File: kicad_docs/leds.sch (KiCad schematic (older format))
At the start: 13 parts, among them U12 74HC595

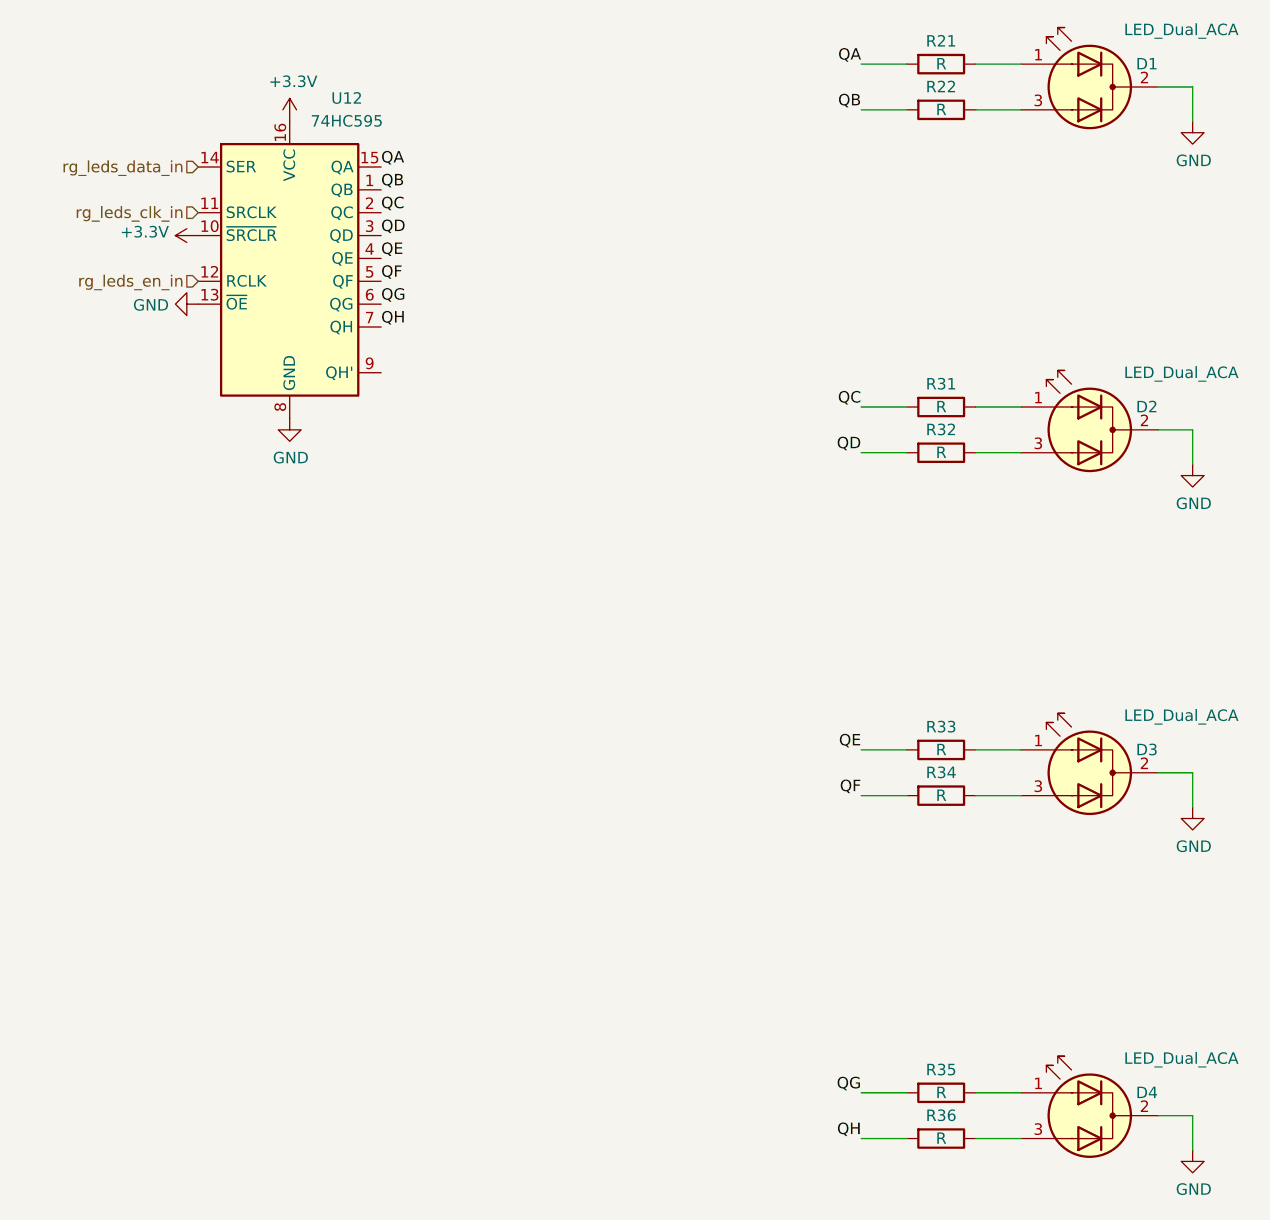
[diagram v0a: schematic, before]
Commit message: add EEPROM, big pcb re-design
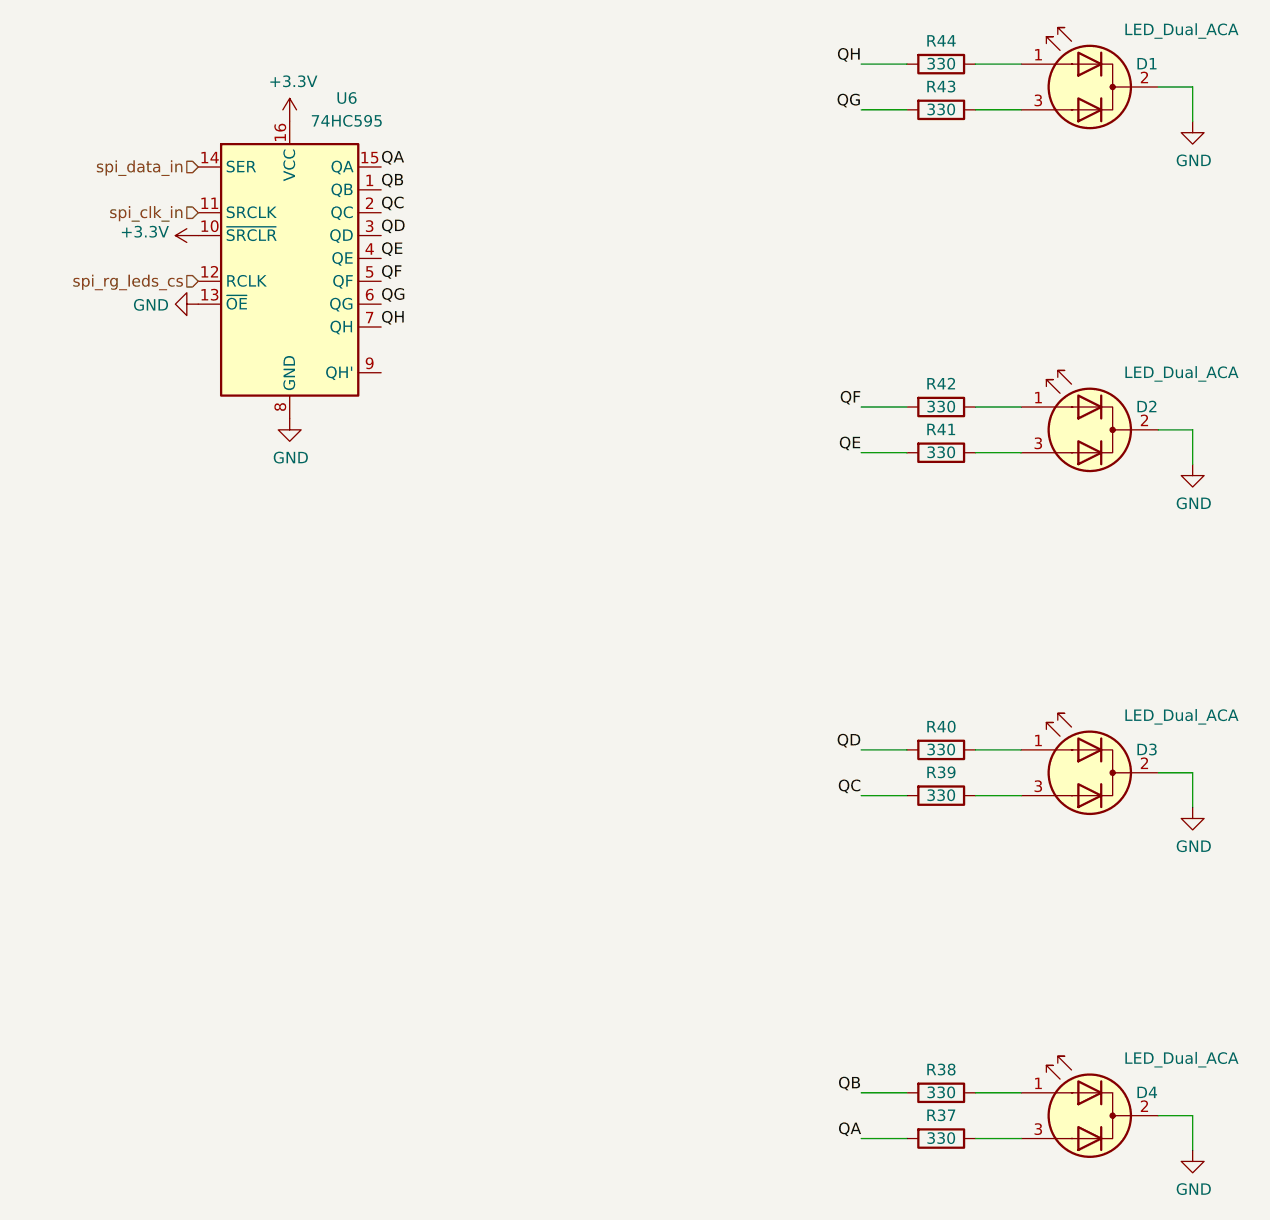
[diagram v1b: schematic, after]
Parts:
- R37: renamed from R21; value R -> 330; footprint Resistor_SMD:R_0805_2012Metric_Pad1.15x1.40mm_HandSolder -> Resistor_SMD:R_0603_1608Metric
- R38: renamed from R22; value R -> 330; footprint Resistor_SMD:R_0805_2012Metric_Pad1.15x1.40mm_HandSolder -> Resistor_SMD:R_0603_1608Metric
- R39: renamed from R31; value R -> 330; footprint Resistor_SMD:R_0805_2012Metric_Pad1.15x1.40mm_HandSolder -> Resistor_SMD:R_0603_1608Metric
- R40: renamed from R32; value R -> 330; footprint Resistor_SMD:R_0805_2012Metric_Pad1.15x1.40mm_HandSolder -> Resistor_SMD:R_0603_1608Metric
- R41: renamed from R33; value R -> 330; footprint Resistor_SMD:R_0805_2012Metric_Pad1.15x1.40mm_HandSolder -> Resistor_SMD:R_0603_1608Metric
- R42: renamed from R34; value R -> 330; footprint Resistor_SMD:R_0805_2012Metric_Pad1.15x1.40mm_HandSolder -> Resistor_SMD:R_0603_1608Metric
- R43: renamed from R35; value R -> 330; footprint Resistor_SMD:R_0805_2012Metric_Pad1.15x1.40mm_HandSolder -> Resistor_SMD:R_0603_1608Metric
- R44: renamed from R36; value R -> 330; footprint Resistor_SMD:R_0805_2012Metric_Pad1.15x1.40mm_HandSolder -> Resistor_SMD:R_0603_1608Metric
- renumbered U12 to U6
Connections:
- net at D1.1 (A1): now also R44.1; no longer R37.1
- net at D1.3 (A2): now also R43.1; no longer R38.1
- net at D2.1 (A1): now also R42.1; no longer R39.1
- net at D2.3 (A2): now also R41.1; no longer R40.1
- net at D3.1 (A1): now also R40.1; no longer R41.1
- net at D3.3 (A2): now also R39.1; no longer R42.1
- net at D4.1 (A1): now also R38.1; no longer R43.1
- net at D4.3 (A2): now also R37.1; no longer R44.1
- net rg_leds_clk_in renamed spi_clk_in
- net rg_leds_data_in renamed spi_data_in
- net rg_leds_en_in renamed spi_rg_leds_cs
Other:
- moved on the sheet: R37, R38, R39, R40, R41, R42, R43, R44
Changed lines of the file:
@@
 $Descr A4 11693 8268
 encoding utf-8
-Sheet 4 9
+Sheet 10 10
 Title ""
 Date ""
@@
 $EndComp
 $Comp
-L Device:R R21
+L Device:R R37
 U 1 1 5E6471EE
+P 6000 6150
+F 0 "R37" V 5900 6150 50  0000 C CNN
+F 1 "330" V 6000 6150 50  0000 C CNN
+F 2 "Resistor_SMD:R_0603_1608Metric" V 5930 6150 50  0001 C CNN
+F 3 "~" H 6000 6150 50  0001 C CNN
+	1    6000 6150
+	0    1    1    0
+$EndComp
+$Comp
+L Device:R R38
+U 1 1 5E6477D0
+P 6000 5950
+F 0 "R38" V 5900 5950 50  0000 C CNN
+F 1 "330" V 6000 5950 50  0000 C CNN
+F 2 "Resistor_SMD:R_0603_1608Metric" V 5930 5950 50  0001 C CNN
+F 3 "~" H 6000 5950 50  0001 C CNN
+	1    6000 5950
+	0    1    1    0
+$EndComp
+Wire Wire Line
+	6350 1450 6150 1450
+Wire Wire Line
+	5850 6150 5650 6150
+Wire Wire Line
+	5650 5950 5850 5950
+Wire Wire Line
+	6150 1650 6350 1650
+$Comp
+L Device:R R39
+U 1 1 5E7B2863
+P 6000 4650
+F 0 "R39" V 5900 4650 50  0000 C CNN
+F 1 "330" V 6000 4650 50  0000 C CNN
+F 2 "Resistor_SMD:R_0603_1608Metric" V 5930 4650 50  0001 C CNN
+F 3 "~" H 6000 4650 50  0001 C CNN
+	1    6000 4650
+	0    1    1    0
+$EndComp
+$Comp
+L Device:R R40
+U 1 1 5E7B2869
+P 6000 4450
+F 0 "R40" V 5900 4450 50  0000 C CNN
+F 1 "330" V 6000 4450 50  0000 C CNN
+F 2 "Resistor_SMD:R_0603_1608Metric" V 5930 4450 50  0001 C CNN
+F 3 "~" H 6000 4450 50  0001 C CNN
+	1    6000 4450
+	0    1    1    0
+$EndComp
+Wire Wire Line
+	6350 2950 6150 2950
+Wire Wire Line
+	5850 4650 5650 4650
+Wire Wire Line
+	5650 4450 5850 4450
+Wire Wire Line
+	6150 3150 6350 3150
+$Comp
+L Device:R R41
+U 1 1 5E7B36D9
+P 6000 3150
+F 0 "R41" V 5900 3150 50  0000 C CNN
+F 1 "330" V 6000 3150 50  0000 C CNN
+F 2 "Resistor_SMD:R_0603_1608Metric" V 5930 3150 50  0001 C CNN
+F 3 "~" H 6000 3150 50  0001 C CNN
+	1    6000 3150
+	0    1    1    0
+$EndComp
+$Comp
+L Device:R R42
+U 1 1 5E7B36DF
+P 6000 2950
+F 0 "R42" V 5900 2950 50  0000 C CNN
+F 1 "330" V 6000 2950 50  0000 C CNN
+F 2 "Resistor_SMD:R_0603_1608Metric" V 5930 2950 50  0001 C CNN
+F 3 "~" H 6000 2950 50  0001 C CNN
+	1    6000 2950
+	0    1    1    0
+$EndComp
+Wire Wire Line
+	6350 4450 6150 4450
+Wire Wire Line
+	5850 3150 5650 3150
+Wire Wire Line
+	5650 2950 5850 2950
+Wire Wire Line
+	6150 4650 6350 4650
+$Comp
+L Device:R R43
+U 1 1 5E7B44F9
+P 6000 1650
+F 0 "R43" V 5900 1650 50  0000 C CNN
+F 1 "330" V 6000 1650 50  0000 C CNN
+F 2 "Resistor_SMD:R_0603_1608Metric" V 5930 1650 50  0001 C CNN
+F 3 "~" H 6000 1650 50  0001 C CNN
+	1    6000 1650
+	0    1    1    0
+$EndComp
+$Comp
+L Device:R R44
+U 1 1 5E7B44FF
 P 6000 1450
-F 0 "R21" V 5900 1450 50  0000 C CNN
-F 1 "R" V 6000 1450 50  0000 C CNN
-F 2 "Resistor_SMD:R_0805_2012Metric_Pad1.15x1.40mm_HandSolder" V 5930 1450 50  0001 C CNN
+F 0 "R44" V 5900 1450 50  0000 C CNN
+F 1 "330" V 6000 1450 50  0000 C CNN
+F 2 "Resistor_SMD:R_0603_1608Metric" V 5930 1450 50  0001 C CNN
 F 3 "~" H 6000 1450 50  0001 C CNN
 	1    6000 1450
 	0    1    1    0
 $EndComp
-$Comp
-L Device:R R22
-U 1 1 5E6477D0
-P 6000 1650
-F 0 "R22" V 5900 1650 50  0000 C CNN
-F 1 "R" V 6000 1650 50  0000 C CNN
-F 2 "Resistor_SMD:R_0805_2012Metric_Pad1.15x1.40mm_HandSolder" V 5930 1650 50  0001 C CNN
-F 3 "~" H 6000 1650 50  0001 C CNN
-	1    6000 1650
-	0    1    1    0
-$EndComp
-Wire Wire Line
-	6350 1450 6150 1450
-Wire Wire Line
-	5850 1450 5650 1450
-Wire Wire Line
-	5650 1650 5850 1650
-Wire Wire Line
-	6150 1650 6350 1650
-$Comp
-L Device:R R31
-U 1 1 5E7B2863
-P 6000 2950
-F 0 "R31" V 5900 2950 50  0000 C CNN
-F 1 "R" V 6000 2950 50  0000 C CNN
-F 2 "Resistor_SMD:R_0805_2012Metric_Pad1.15x1.40mm_HandSolder" V 5930 2950 50  0001 C CNN
-F 3 "~" H 6000 2950 50  0001 C CNN
-	1    6000 2950
-	0    1    1    0
-$EndComp
-$Comp
-L Device:R R32
-U 1 1 5E7B2869
-P 6000 3150
-F 0 "R32" V 5900 3150 50  0000 C CNN
-F 1 "R" V 6000 3150 50  0000 C CNN
-F 2 "Resistor_SMD:R_0805_2012Metric_Pad1.15x1.40mm_HandSolder" V 5930 3150 50  0001 C CNN
-F 3 "~" H 6000 3150 50  0001 C CNN
-	1    6000 3150
-	0    1    1    0
-$EndComp
-Wire Wire Line
-	6350 2950 6150 2950
-Wire Wire Line
-	5850 2950 5650 2950
-Wire Wire Line
-	5650 3150 5850 3150
-Wire Wire Line
-	6150 3150 6350 3150
-$Comp
-L Device:R R33
-U 1 1 5E7B36D9
-P 6000 4450
-F 0 "R33" V 5900 4450 50  0000 C CNN
-F 1 "R" V 6000 4450 50  0000 C CNN
-F 2 "Resistor_SMD:R_0805_2012Metric_Pad1.15x1.40mm_HandSolder" V 5930 4450 50  0001 C CNN
-F 3 "~" H 6000 4450 50  0001 C CNN
-	1    6000 4450
-	0    1    1    0
-$EndComp
-$Comp
-L Device:R R34
-U 1 1 5E7B36DF
-P 6000 4650
-F 0 "R34" V 5900 4650 50  0000 C CNN
-F 1 "R" V 6000 4650 50  0000 C CNN
-F 2 "Resistor_SMD:R_0805_2012Metric_Pad1.15x1.40mm_HandSolder" V 5930 4650 50  0001 C CNN
-F 3 "~" H 6000 4650 50  0001 C CNN
-	1    6000 4650
-	0    1    1    0
-$EndComp
-Wire Wire Line
-	6350 4450 6150 4450
-Wire Wire Line
-	5850 4450 5650 4450
-Wire Wire Line
-	5650 4650 5850 4650
-Wire Wire Line
-	6150 4650 6350 4650
-$Comp
-L Device:R R35
-U 1 1 5E7B44F9
-P 6000 5950
-F 0 "R35" V 5900 5950 50  0000 C CNN
-F 1 "R" V 6000 5950 50  0000 C CNN
-F 2 "Resistor_SMD:R_0805_2012Metric_Pad1.15x1.40mm_HandSolder" V 5930 5950 50  0001 C CNN
-F 3 "~" H 6000 5950 50  0001 C CNN
-	1    6000 5950
-	0    1    1    0
-$EndComp
-$Comp
-L Device:R R36
-U 1 1 5E7B44FF
-P 6000 6150
-F 0 "R36" V 5900 6150 50  0000 C CNN
-F 1 "R" V 6000 6150 50  0000 C CNN
-F 2 "Resistor_SMD:R_0805_2012Metric_Pad1.15x1.40mm_HandSolder" V 5930 6150 50  0001 C CNN
-F 3 "~" H 6000 6150 50  0001 C CNN
-	1    6000 6150
-	0    1    1    0
-$EndComp
 Wire Wire Line
 	6350 5950 6150 5950
 Wire Wire Line
-	5850 5950 5650 5950
-Wire Wire Line
-	5650 6150 5850 6150
+	5850 1650 5650 1650
+Wire Wire Line
+	5650 1450 5850 1450
 Wire Wire Line
 	6150 6150 6350 6150
 $Comp
-L power:GND #PWR034
+L power:GND #PWR033
 U 1 1 5E7B9CAD
 P 7100 1700
-F 0 "#PWR034" H 7100 1450 50  0001 C CNN
+F 0 "#PWR033" H 7100 1450 50  0001 C CNN
 F 1 "GND" H 7105 1527 50  0000 C CNN
 F 2 "" H 7100 1700 50  0001 C CNN
@@
 	7100 1550 6950 1550
 $Comp
-L power:GND #PWR035
+L power:GND #PWR034
 U 1 1 5E7BADED
 P 7100 3200
-F 0 "#PWR035" H 7100 2950 50  0001 C CNN
+F 0 "#PWR034" H 7100 2950 50  0001 C CNN
 F 1 "GND" H 7105 3027 50  0000 C CNN
 F 2 "" H 7100 3200 50  0001 C CNN
@@
 	7100 3050 6950 3050
 $Comp
-L power:GND #PWR036
+L power:GND #PWR035
 U 1 1 5E7BB8B1
 P 7100 4700
-F 0 "#PWR036" H 7100 4450 50  0001 C CNN
+F 0 "#PWR035" H 7100 4450 50  0001 C CNN
 F 1 "GND" H 7105 4527 50  0000 C CNN
 F 2 "" H 7100 4700 50  0001 C CNN
@@
 	7100 4550 6950 4550
 $Comp
-L power:GND #PWR037
+L power:GND #PWR036
 U 1 1 5E7BC1EC
 P 7100 6200
-F 0 "#PWR037" H 7100 5950 50  0001 C CNN
+F 0 "#PWR036" H 7100 5950 50  0001 C CNN
 F 1 "GND" H 7105 6027 50  0000 C CNN
 F 2 "" H 7100 6200 50  0001 C CNN
@@
 	7100 6050 6950 6050
 $Comp
-L 74xx:74HC595 U12
+L 74xx:74HC595 U6
 U 1 1 5E7AE971
 P 3150 2300
-F 0 "U12" H 3400 3000 50  0000 C CNN
+F 0 "U6" H 3400 3000 50  0000 C CNN
 F 1 "74HC595" H 3400 2900 50  0000 C CNN
 F 2 "Package_SO:SOIC-16_3.9x9.9mm_P1.27mm" H 3150 2300 50  0001 C CNN
@@
 $EndComp
 Text HLabel 2750 1900 0    50   Input ~ 0
-rg_leds_data_in
+spi_data_in
 Text HLabel 2750 2100 0    50   Input ~ 0
-rg_leds_clk_in
+spi_clk_in
 Text Label 3550 1900 0    50   ~ 0
 QA
@@
 Text Label 3550 2600 0    50   ~ 0
 QH
-Text Label 5650 1450 2    50   ~ 0
-QA
-Text Label 5650 1650 2    50   ~ 0
-QB
-Text Label 5650 2950 2    50   ~ 0
-QC
-Text Label 5650 3150 2    50   ~ 0
-QD
-Text Label 5650 4450 2    50   ~ 0
-QE
-Text Label 5650 4650 2    50   ~ 0
-QF
-Text Label 5650 5950 2    50   ~ 0
-QG
-Text Label 5650 6150 2    50   ~ 0
-QH
-$Comp
-L power:+3.3V #PWR0103
+$Comp
+L power:+3.3V #PWR031
 U 1 1 5E7CB872
 P 3150 1700
-F 0 "#PWR0103" H 3150 1550 50  0001 C CNN
+F 0 "#PWR031" H 3150 1550 50  0001 C CNN
 F 1 "+3.3V" H 3165 1873 50  0000 C CNN
 F 2 "" H 3150 1700 50  0001 C CNN
@@
 $EndComp
 $Comp
-L power:GND #PWR0104
+L power:GND #PWR032
 U 1 1 5E7CCA2D
 P 3150 3000
-F 0 "#PWR0104" H 3150 2750 50  0001 C CNN
+F 0 "#PWR032" H 3150 2750 50  0001 C CNN
 F 1 "GND" H 3155 2827 50  0000 C CNN
 F 2 "" H 3150 3000 50  0001 C CNN
@@
 $EndComp
 $Comp
-L power:GND #PWR0107
+L power:GND #PWR030
 U 1 1 5E8083F0
 P 2750 2500
-F 0 "#PWR0107" H 2750 2250 50  0001 C CNN
+F 0 "#PWR030" H 2750 2250 50  0001 C CNN
 F 1 "GND" V 2755 2372 50  0000 R CNN
 F 2 "" H 2750 2500 50  0001 C CNN
@@
 $EndComp
 $Comp
-L power:+3.3V #PWR0108
+L power:+3.3V #PWR029
 U 1 1 5E80873A
 P 2750 2200
-F 0 "#PWR0108" H 2750 2050 50  0001 C CNN
+F 0 "#PWR029" H 2750 2050 50  0001 C CNN
 F 1 "+3.3V" V 2765 2328 50  0000 L CNN
 F 2 "" H 2750 2200 50  0001 C CNN
@@
 $EndComp
 Text HLabel 2750 2400 0    50   Input ~ 0
-rg_leds_en_in
+spi_rg_leds_cs
+Text Label 5650 4450 2    50   ~ 0
+QD
+Text Label 5650 3150 2    50   ~ 0
+QE
+Text Label 5650 2950 2    50   ~ 0
+QF
+Text Label 5650 4650 2    50   ~ 0
+QC
+Text Label 5650 5950 2    50   ~ 0
+QB
+Text Label 5650 1650 2    50   ~ 0
+QG
+Text Label 5650 6150 2    50   ~ 0
+QA
+Text Label 5650 1450 2    50   ~ 0
+QH
 $EndSCHEMATC
